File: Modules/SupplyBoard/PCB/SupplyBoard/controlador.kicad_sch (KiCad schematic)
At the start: 1 part, among them U1 STM32L031G6Ux

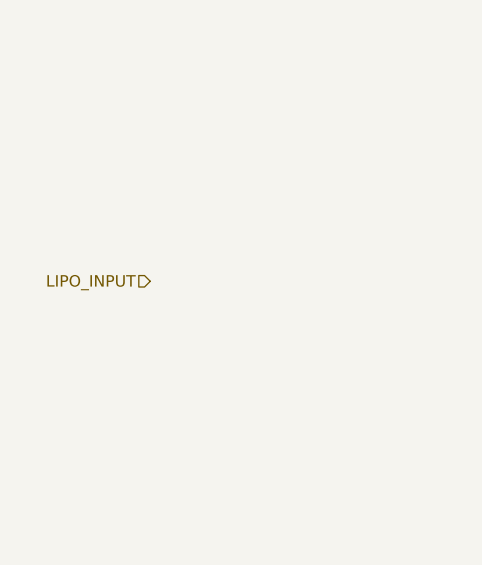
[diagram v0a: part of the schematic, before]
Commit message: SupplyBoard - Added INA2180 current sensor
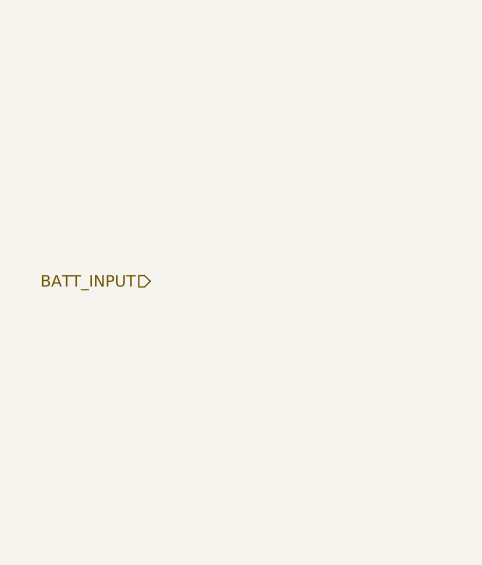
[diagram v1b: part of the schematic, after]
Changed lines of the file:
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@@
 		)
 	)
-	(hierarchical_label "LIPO_INPUT"
+	(hierarchical_label "BATT_INPUT"
 		(shape input)
 		(at 78.74 74.93 180)

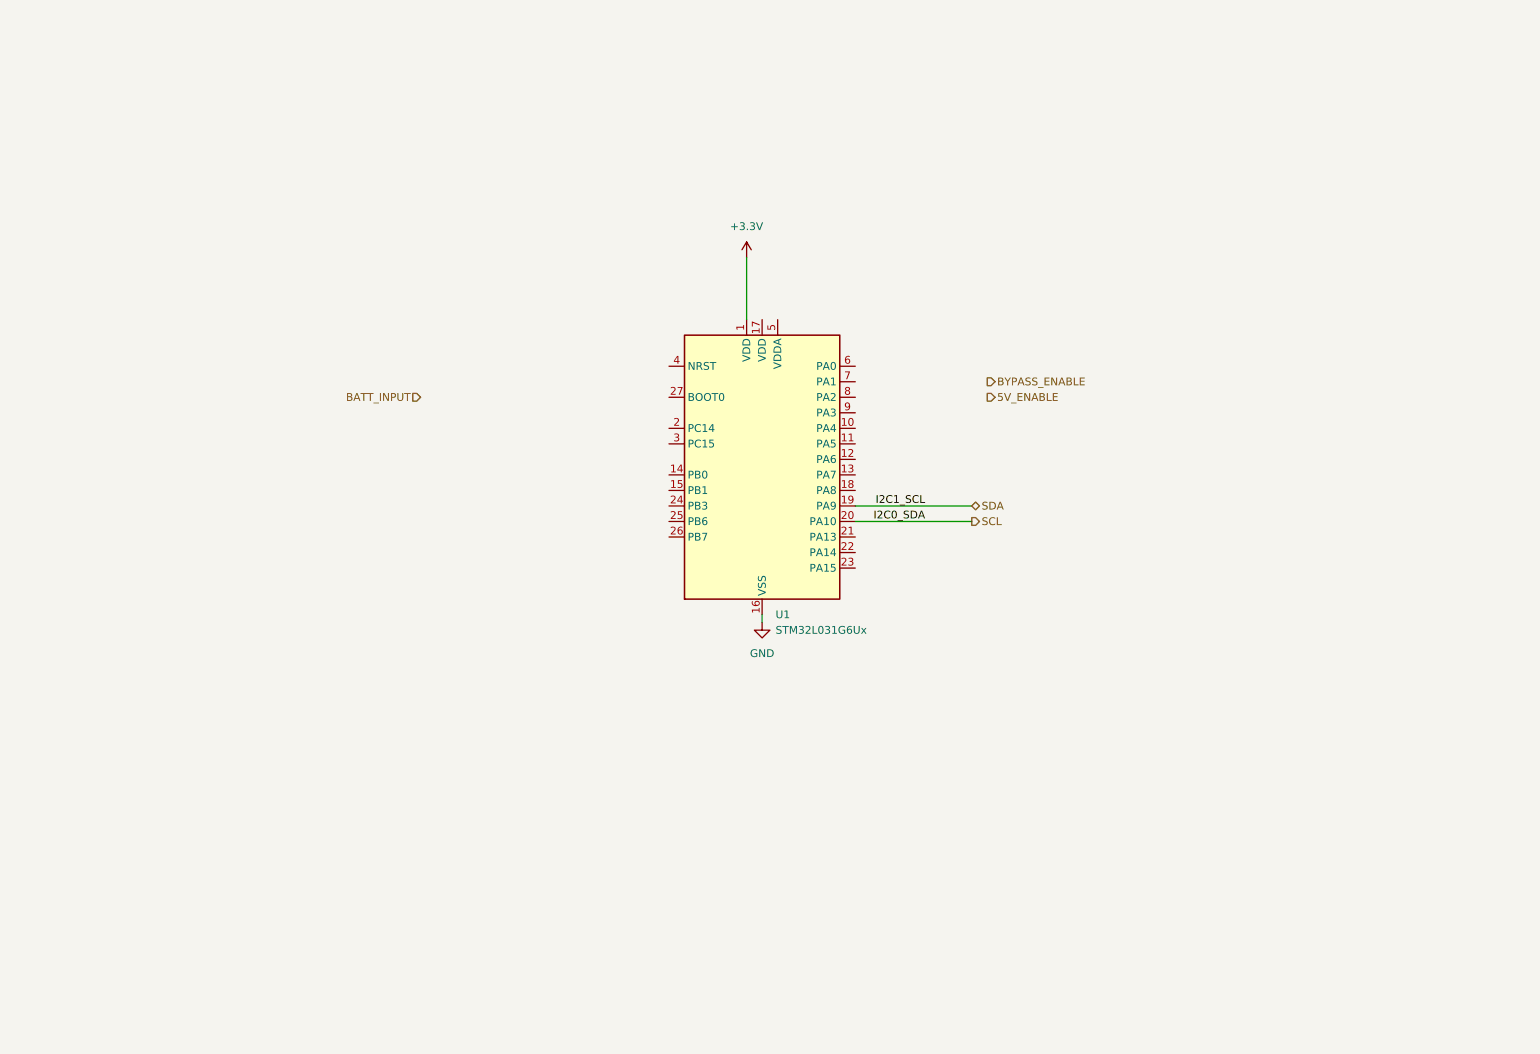
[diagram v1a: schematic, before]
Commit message: Supply board schematic and PCB
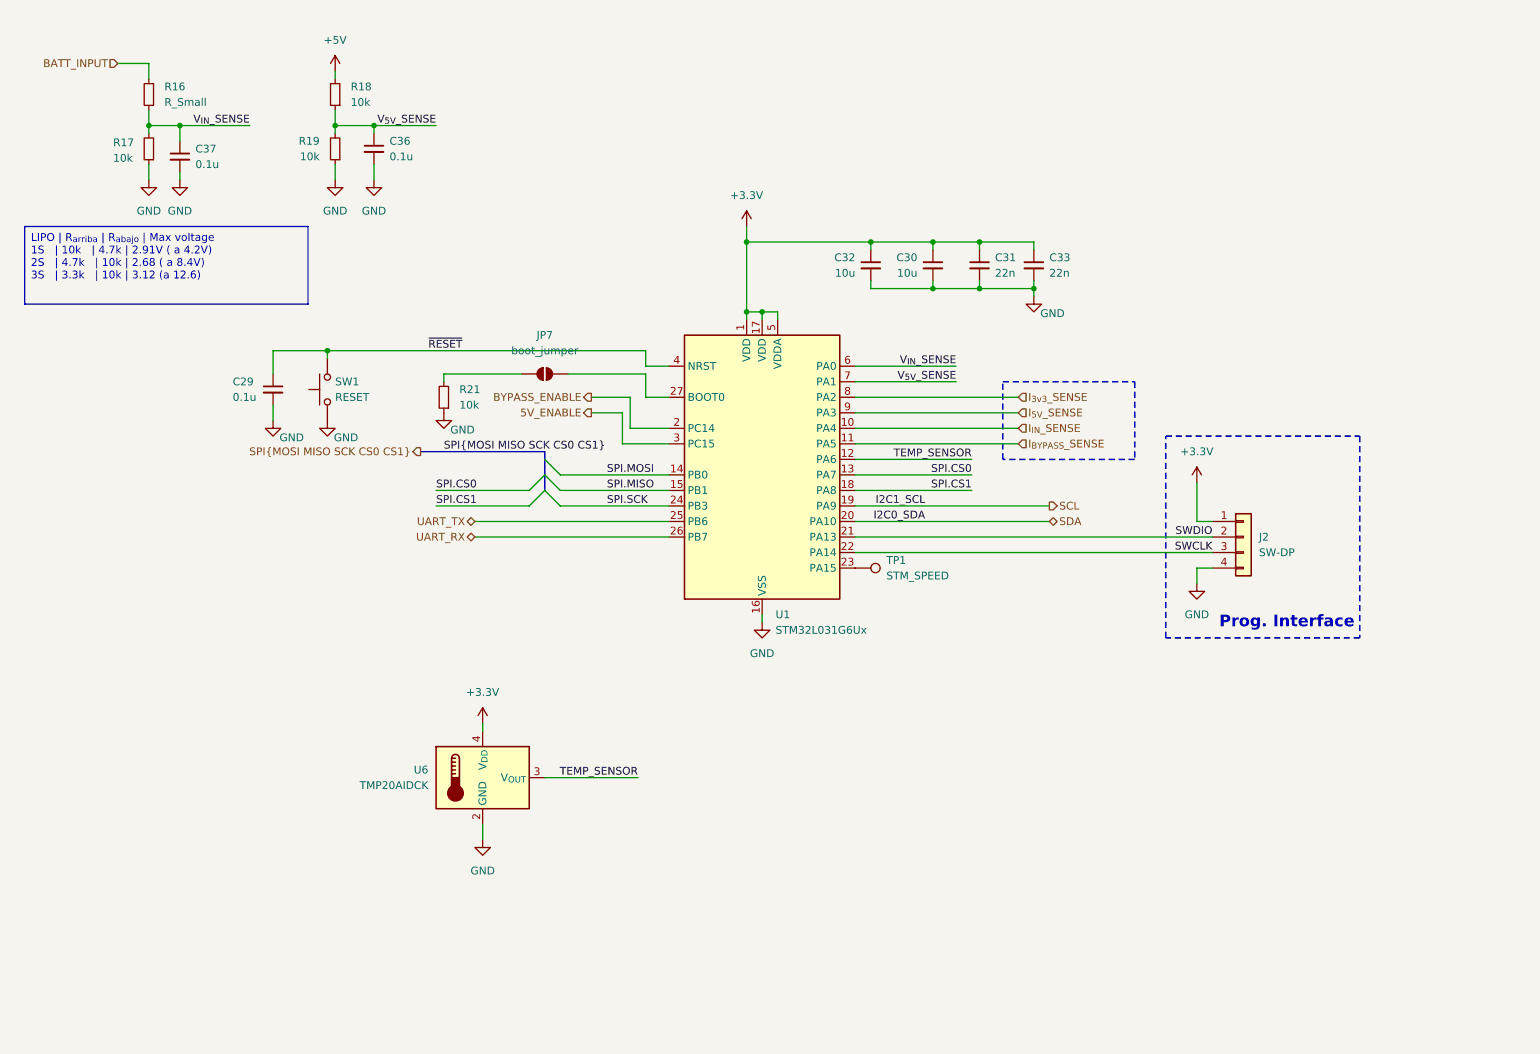
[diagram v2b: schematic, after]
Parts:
- added C29, C36, C37: 0.1u, Capacitor_SMD:C_0603_1608Metric_Pad1.08x0.95mm_HandSolder, symbol Device:C_Small
- added C30, C32: 10u, Capacitor_SMD:C_0603_1608Metric_Pad1.08x0.95mm_HandSolder, symbol Device:C_Small
- added C31, C33: 22n, Capacitor_SMD:C_0603_1608Metric_Pad1.08x0.95mm_HandSolder, symbol Device:C_Small
- added J2: SW-DP, Connector_PinHeader_2.54mm:PinHeader_1x04_P2.54mm_Vertical, symbol Connector_Generic:Conn_01x04
- added JP7: boot_jumper, Jumper:SolderJumper-2_P1.3mm_Open_RoundedPad1.0x1.5mm, symbol Jumper:SolderJumper_2_Open
- added R16: R_Small, Resistor_SMD:R_0603_1608Metric_Pad0.98x0.95mm_HandSolder, symbol Device:R_Small
- added R17, R18, R19, R21: 10k, Resistor_SMD:R_0603_1608Metric_Pad0.98x0.95mm_HandSolder, symbol Device:R_Small
- added SW1: RESET, IcaroFootprints:SideSwitch_2.7_4.65, symbol Switch:SW_Push
- added TP1: STM_SPEED, symbol Connector:TestPoint
- added U6: TMP20AIDCK, Package_TO_SOT_SMD:SOT-353_SC-70-5, symbol Sensor_Temperature:TMP20AIDCK
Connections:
- net +3.3V: now also U1.17 (VDD), U1.5 (VDDA), C30.1, C31.1, C32.1, C33.1, J2.1 (Pin_1), U6.4 (V_{DD})
- net 5V_ENABLE: now also U1.3 (PC15)
- net BATT_INPUT: now also R16.2
- net BYPASS_ENABLE: now also U1.2 (PC14)
- net GND: now also C29.2, C30.2, C31.2, C32.2, C33.2, C36.2, C37.2, J2.4 (Pin_4), R17.1, R19.1, R21.1, SW1.1, U6.2 (GND), U6.5 (GND)
- net SCL: now also U1.19 (PA9); no longer U1.20 (PA10)
- net SDA: now also U1.20 (PA10); no longer U1.19 (PA9)
- net I_{IN}_SENSE: now reaches U1.10 (PA4)
- net I_{BYPASS}_SENSE: now reaches U1.11 (PA5)
- net TEMP_SENSOR: now reaches U1.12 (PA6)
- net TEMP_SENSOR: now also U6.3 (V_{OUT})
- net SPI.CS0: now reaches U1.13 (PA7)
- net SPI.MOSI: now reaches U1.14 (PB0)
- net SPI.MISO: now reaches U1.15 (PB1)
- net SPI.CS1: now reaches U1.18 (PA8)
- net SWDIO: now reaches U1.21 (PA13)
- net SWDIO: now also J2.2 (Pin_2)
- net SWCLK: now reaches U1.22 (PA14)
- net SWCLK: now also J2.3 (Pin_3)
- net at U1.23 (PA15): now also TP1.1
- net SPI.SCK: now reaches U1.24 (PB3)
- net UART_TX: now reaches U1.25 (PB6)
- net UART_RX: now reaches U1.26 (PB7)
- net at U1.27 (BOOT0): now also JP7.2 (B)
- net ~{RESET}: now reaches U1.4 (NRST)
- net ~{RESET}: now also C29.1, SW1.2
- net V_{IN}_SENSE: now reaches U1.6 (PA0)
- net V_{IN}_SENSE: now also C37.1, R16.1, R17.2
- net V_{5V}_SENSE: now reaches U1.7 (PA1)
- net V_{5V}_SENSE: now also C36.1, R18.1, R19.2
- net I_{3v3}_SENSE: now reaches U1.8 (PA2)
- net I_{5V}_SENSE: now reaches U1.9 (PA3)
- new net: JP7.1 (A), R21.2
- new net +5V: R18.2
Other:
- note added: "Prog. Interface"

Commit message: Muchas cosas: Backplane, SupplyBoard y principio SensorBoard
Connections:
- net SPI.MISO: now also U1.14 (PB0); no longer U1.15 (PB1)
- net SPI.MOSI: now also U1.15 (PB1); no longer U1.14 (PB0)
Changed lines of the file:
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@@
 	)
 	(label "SPI.MOSI"
-		(at 109.22 87.63 0)
+		(at 109.22 90.17 0)
 		(effects
 			(font
@@
 	)
 	(label "SPI.MISO"
-		(at 109.22 90.17 0)
+		(at 109.22 87.63 0)
 		(effects
 			(font

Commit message: Finished Supply board
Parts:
- TP1: footprint (none) -> TestPoint:TestPoint_Pad_D1.5mm
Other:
- moved on the sheet: C29, C30, C31, C32, C33, C36, C37, J2, JP7, R16, R17, R18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

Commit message: Working GPIO and ADC
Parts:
- U6: value TMP20AIDCK -> TMP235A4DCKR
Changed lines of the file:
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@@
 			)
 		)
-		(property "Value" "TMP20AIDCK"
+		(property "Value" "TMP235A4DCKR"
 			(at 48.26 165.0999 0)
 			(effects
@@
 			)
 		)
-		(property "Datasheet" "http://www.ti.com/lit/ds/symlink/tmp20.pdf"
+		(property "Datasheet" "https://www.ti.com/lit/ds/symlink/tmp235.pdf?ts=1742153153204&ref_url=https%253A%252F%252Fwww.ti.com%252Fproduct%252Fes-mx%252FTMP235"
 			(at 57.15 163.83 0)
 			(effects
@@
 		(fields_autoplaced yes)
 		(property "Reference" "U1"
-			(at 162.2141 119.38 0)
+			(at 162.1633 119.38 0)
 			(effects
 				(font
@@
 		)
 		(property "Value" "STM32L031G6Ux"
-			(at 162.2141 121.92 0)
+			(at 162.1633 121.92 0)
 			(effects
 				(font
